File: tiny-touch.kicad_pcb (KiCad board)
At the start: 2 copper layers, 0 parts

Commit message: Begin PCB layout
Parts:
- added 12: Tiny-Touch-Pad, ckeys:Tiny-Touch-Pad, F.Cu at (197.9, 122.4)
- added C1: 1UF, Capacitor_SMD:C_0603_1608Metric_Pad1.05x0.95mm_HandSolder, F.Cu at (262.0, 180.3)
- added C10: 4.7nF, Capacitor_SMD:C_0603_1608Metric_Pad1.05x0.95mm_HandSolder, F.Cu at (243.9, 195.6)
- added C11: 4.7nF, Capacitor_SMD:C_0603_1608Metric_Pad1.05x0.95mm_HandSolder, F.Cu at (257.7, 180.3)
- added C2: 1UF, Capacitor_SMD:C_0603_1608Metric_Pad1.05x0.95mm_HandSolder, F.Cu at (248.3, 193.0)
- added C3: 0.1UF, Capacitor_SMD:C_0603_1608Metric_Pad1.05x0.95mm_HandSolder, F.Cu at (263.1, 173.2)
- added C4: 4.7UF, Capacitor_SMD:C_0603_1608Metric_Pad1.05x0.95mm_HandSolder, F.Cu at (198.1, 204.2)
- added C5: 1UF, Capacitor_SMD:C_0603_1608Metric_Pad1.05x0.95mm_HandSolder, F.Cu at (239.6, 193.0)
- added C6: 10UF, Capacitor_SMD:C_0603_1608Metric_Pad1.05x0.95mm_HandSolder, F.Cu at (239.6, 195.6)
- added C7: 0.1UF, Capacitor_SMD:C_0603_1608Metric_Pad1.05x0.95mm_HandSolder, F.Cu at (258.2, 177.8)
- added C8: 0.1UF, Capacitor_SMD:C_0603_1608Metric_Pad1.05x0.95mm_HandSolder, F.Cu at (243.9, 193.0)
- added C9: 4.7UF, Capacitor_SMD:C_0603_1608Metric_Pad1.05x0.95mm_HandSolder, F.Cu at (262.6, 177.8)
- added D1: RB060M-60TR, ckeys:PMDU, F.Cu at (184.0, 179.8)
- added D2: 1N4148, Diode_SMD:D_SOD-323_HandSoldering, F.Cu at (195.5, 153.8)
- added F1: Tiny-Touch-Pad, ckeys:Tiny-Touch-Pad, F.Cu at (126.3, 122.4)
- added F10: Tiny-Touch-Pad, ckeys:Tiny-Touch-Pad, F.Cu at (184.9, 122.3)
- added F11: Tiny-Touch-Pad, ckeys:Tiny-Touch-Pad, F.Cu at (191.4, 122.4)
- added F2: Tiny-Touch-Pad, ckeys:Tiny-Touch-Pad, F.Cu at (132.8, 122.4)
- added F3: Tiny-Touch-Pad, ckeys:Tiny-Touch-Pad, F.Cu at (139.4, 122.4)
- added F4: Tiny-Touch-Pad, ckeys:Tiny-Touch-Pad, F.Cu at (145.9, 122.4)
- added F5: Tiny-Touch-Pad, ckeys:Tiny-Touch-Pad, F.Cu at (152.4, 122.3)
- added F6: Tiny-Touch-Pad, ckeys:Tiny-Touch-Pad, F.Cu at (158.9, 122.3)
- added F7: Tiny-Touch-Pad, ckeys:Tiny-Touch-Pad, F.Cu at (165.4, 122.3)
- added F8: Tiny-Touch-Pad, ckeys:Tiny-Touch-Pad, F.Cu at (171.9, 122.3)
- added F9: Tiny-Touch-Pad, ckeys:Tiny-Touch-Pad, F.Cu at (178.4, 122.3)
- added H1: Pointer_Clip, ckeys:microbit-clamp-hole-pad, F.Cu at (179.0, 174.2)
- added IC1: STM32F072VBT6, ckeys:QFP50P1600X1600X160-100N, F.Cu at (184.6, 161.3)
- added PAD13: Tiny-Touch-Pad, ckeys:Tiny-Touch-Pad-2u, F.Cu at (206.6, 122.5)
- added PAD14: Tiny-Touch-Pad, ckeys:Tiny-Touch-Pad-2u, F.Cu at (128.6, 129.1)
- added PAD15: Tiny-Touch-Pad, ckeys:Tiny-Touch-Pad-2u, F.Cu at (139.1, 129.1)
- added PAD16: Tiny-Touch-Pad, ckeys:Tiny-Touch-Pad-3u, F.Cu at (156.1, 136.6)
- added PAD17: Tiny-Touch-Pad, ckeys:Tiny-Touch-Pad-1.75u, F.Cu at (170.7, 136.6)
- added PAD18: Tiny-Touch-Pad, ckeys:Tiny-Touch-Pad-1.75u, F.Cu at (149.2, 178.5)
- added PAD19: Tiny-Touch-Pad, ckeys:Tiny-Touch-Pad-1.75u, F.Cu at (158.1, 178.5)
- added PAD20: Tiny-Touch-Pad, ckeys:Tiny-Touch-Pad-1.75u, F.Cu at (156.8, 191.2)
- added PAD21: Tiny-Touch-Pad, ckeys:Tiny-Touch-Pad-2u, F.Cu at (167.2, 188.6)
- added PAD22: Tiny-Touch-Pad, ckeys:Tiny-Touch-Pad-1.5u, F.Cu at (166.0, 196.2)
- added PAD23: Tiny-Touch-Pad, ckeys:Tiny-Touch-Pad-1.5u, F.Cu at (166.0, 202.6)
- added PAD24: Tiny-Touch-Pad, ckeys:Tiny-Touch-Pad-2.25u, F.Cu at (220.5, 152.8)
- added PAD25: Tiny-Touch-Pad, ckeys:Tiny-Touch-Pad-2.25u, F.Cu at (154.5, 209.0)
- added PAD26: Tiny-Touch-Pad, ckeys:Tiny-Touch-Pad-2.25u, F.Cu at (163.4, 209.0)
- added PAD27: Tiny-Touch-Pad, ckeys:Tiny-Touch-Pad-2.25u, F.Cu at (181.6, 198.1)
- added PAD28: Tiny-Touch-Pad, ckeys:Tiny-Touch-Pad, F.Cu at (205.5, 193.5)
- added PAD29: Tiny-Touch-Pad, ckeys:Tiny-Touch-Pad, F.Cu at (240.6, 149.0)
- added PAD30: Tiny-Touch-Pad, ckeys:Tiny-Touch-Pad, F.Cu at (200.5, 197.1)
- added PAD31: Tiny-Touch-Pad, ckeys:Tiny-Touch-Pad, F.Cu at (210.5, 187.4)
- added PAD32: Tiny-Touch-Pad, ckeys:Tiny-Touch-Pad, F.Cu at (224.1, 178.8)
- added PAD33: Tiny-Touch-Pad, ckeys:Tiny-Touch-Pad, F.Cu at (215.5, 187.4)
- added PAD34: Tiny-Touch-Pad, ckeys:Tiny-Touch-Pad, F.Cu at (243.0, 159.4)
- added PAD35: Tiny-Touch-Pad, ckeys:Tiny-Touch-Pad, F.Cu at (238.0, 166.1)
- added PAD36: Tiny-Touch-Pad, ckeys:Tiny-Touch-Pad, F.Cu at (247.0, 149.0)
- added PAD37: Tiny-Touch-Pad, ckeys:Tiny-Touch-Pad, F.Cu at (229.1, 172.7)
- added PAD38: Tiny-Touch-Pad, ckeys:Tiny-Touch-Pad, F.Cu at (210.5, 194.0)
- added PAD39: Tiny-Touch-Pad, ckeys:Tiny-Touch-Pad, F.Cu at (205.5, 200.1)
- added PAD40: Tiny-Touch-Pad, ckeys:Tiny-Touch-Pad, F.Cu at (224.1, 185.4)
- added PAD41: Tiny-Touch-Pad, ckeys:Tiny-Touch-Pad, F.Cu at (215.5, 194.0)
- added PAD42: Tiny-Touch-Pad, ckeys:Tiny-Touch-Pad-1.5u, F.Cu at (199.4, 184.1)
- added PAD43: Tiny-Touch-Pad, ckeys:Tiny-Touch-Pad, F.Cu at (229.1, 179.3)
- added PAD44: Tiny-Touch-Pad, ckeys:Tiny-Touch-Pad, F.Cu at (255.3, 152.8)
- added PAD45: Tiny-Touch-Pad, ckeys:Tiny-Touch-Pad, F.Cu at (243.0, 166.1)
- added PAD46: Tiny-Touch-Pad, ckeys:Tiny-Touch-Pad, F.Cu at (248.0, 159.4)
- added PAD47: Tiny-Touch-Pad, ckeys:Tiny-Touch-Pad, F.Cu at (210.5, 200.6)
- added PAD48: Tiny-Touch-Pad, ckeys:Tiny-Touch-Pad, F.Cu at (239.1, 172.7)
- added PAD49: Tiny-Touch-Pad, ckeys:Tiny-Touch-Pad, F.Cu at (220.5, 192.0)
- added PAD50: Tiny-Touch-Pad, ckeys:Tiny-Touch-Pad, F.Cu at (215.5, 200.6)
- added PAD51: Tiny-Touch-Pad, ckeys:Tiny-Touch-Pad, F.Cu at (253.0, 159.4)
- added PAD52: Tiny-Touch-Pad, ckeys:Tiny-Touch-Pad, F.Cu at (248.0, 166.1)
- added PAD53: Tiny-Touch-Pad, ckeys:Tiny-Touch-Pad, F.Cu at (260.3, 152.8)
- added PAD54: Tiny-Touch-Pad, ckeys:Tiny-Touch-Pad-1.5u, F.Cu at (208.4, 174.1)
- added PAD55: Tiny-Touch-Pad, ckeys:Tiny-Touch-Pad-1.75u, F.Cu at (207.5, 167.8)
- added PAD56: Tiny-Touch-Pad, ckeys:Tiny-Touch-Pad, F.Cu at (258.0, 159.4)
- added PAD57: Tiny-Touch-Pad, ckeys:Tiny-Touch-Pad, F.Cu at (244.1, 172.7)
- added PAD58: Tiny-Touch-Pad, ckeys:Tiny-Touch-Pad, F.Cu at (239.1, 179.3)
- added PAD59: Tiny-Touch-Pad, ckeys:Tiny-Touch-Pad, F.Cu at (265.3, 152.8)
- added PAD60: Tiny-Touch-Pad, ckeys:Tiny-Touch-Pad, F.Cu at (220.5, 198.6)
- added PAD61: Tiny-Touch-Pad, ckeys:Tiny-Touch-Pad, F.Cu at (253.0, 166.1)
- added PAD62: Tiny-Touch-Pad, ckeys:Tiny-Touch-Pad, F.Cu at (249.1, 172.7)
- added PAD63: Tiny-Touch-Pad, ckeys:Tiny-Touch-Pad, F.Cu at (263.0, 159.4)
- added PAD64: Tiny-Touch-Pad, ckeys:Tiny-Touch-Pad, F.Cu at (234.1, 185.9)
- added PAD65: Tiny-Touch-Pad, ckeys:Tiny-Touch-Pad, F.Cu at (225.5, 192.5)
- added PAD66: Tiny-Touch-Pad, ckeys:Tiny-Touch-Pad, F.Cu at (258.0, 166.1)
- added PAD67: Tiny-Touch-Pad, ckeys:Tiny-Touch-Pad-1.25u, F.Cu at (268.7, 166.1)
- added PAD68: Tiny-Touch-Pad, ckeys:Tiny-Touch-Pad-2.25u, F.Cu at (187.9, 171.3)
- added PAD69: Tiny-Touch-Pad, ckeys:Tiny-Touch-Pad, F.Cu at (244.1, 179.3)
- added PAD70: Tiny-Touch-Pad, ckeys:Tiny-Touch-Pad, F.Cu at (239.1, 185.9)
- added PAD71: Tiny-Touch-Pad, ckeys:Tiny-Touch-Pad, F.Cu at (225.5, 199.2)
- added PAD72: Tiny-Touch-Pad, ckeys:Tiny-Touch-Pad, F.Cu at (249.1, 179.3)
- added PAD73: Tiny-Touch-Pad, ckeys:Tiny-Touch-Pad, F.Cu at (235.5, 192.5)
- added PAD74: Tiny-Touch-Pad, ckeys:Tiny-Touch-Pad, F.Cu at (268.0, 159.4)
- added PAD75: Tiny-Touch-Pad, ckeys:Tiny-Touch-Pad, F.Cu at (254.1, 172.7)
- added PAD76: Tiny-Touch-Pad, ckeys:Tiny-Touch-Pad, F.Cu at (263.0, 166.1)
- added PAD77: Tiny-Touch-Pad, ckeys:Tiny-Touch-Pad, F.Cu at (230.5, 199.2)
- added PAD78: Tiny-Touch-Pad, ckeys:Tiny-Touch-Pad, F.Cu at (244.1, 185.9)
- added PAD79: Tiny-Touch-Pad, ckeys:Tiny-Touch-Pad-1.75u, F.Cu at (216.5, 161.4)
- added PAD80: Tiny-Touch-Pad, ckeys:Tiny-Touch-Pad, F.Cu at (235.5, 199.2)
- added PAD81: Tiny-Touch-Pad, ckeys:Tiny-Touch-Pad, F.Cu at (249.1, 185.9)
- added PAD82: Tiny-Touch-Pad, ckeys:Tiny-Touch-Pad, F.Cu at (270.3, 152.8)
- added PAD83: Tiny-Touch-Pad, ckeys:Tiny-Touch-Pad, F.Cu at (230.5, 192.5)
- added PAD84: Tiny-Touch-Pad, ckeys:Tiny-Touch-Pad, F.Cu at (229.1, 185.9)
- added PAD85: Tiny-Touch-Pad, ckeys:Tiny-Touch-Pad-3u, F.Cu at (199.2, 156.4)
- added PAD86: Tiny-Touch-Pad, ckeys:Tiny-Touch-Pad, F.Cu at (234.1, 179.3)
- added PAD87: Tiny-Touch-Pad, ckeys:Tiny-Touch-Pad, F.Cu at (234.1, 172.7)
- added PAD88: Tiny-Touch-Pad, ckeys:Tiny-Touch-Pad, F.Cu at (219.0, 178.2)
- added PAD89: Tiny-Touch-Pad, ckeys:Tiny-Touch-Pad, F.Cu at (233.0, 166.1)
- added PAD90: Tiny-Touch-Pad, ckeys:Tiny-Touch-Pad, F.Cu at (238.0, 159.4)
- added PAD91: Tiny-Touch-Pad, ckeys:Tiny-Touch-Pad, F.Cu at (224.1, 172.1)
- added PF1: 500mA, Fuse:Fuse_1206_3216Metric_Pad1.42x1.75mm_HandSolder, F.Cu at (189.0, 191.3)
- added Q1: DTC123J, ckeys:SOT65P210X100-3N, F.Cu at (193.6, 204.8)
- added R1: 100K, Resistor_SMD:R_0603_1608Metric_Pad1.05x0.95mm_HandSolder, F.Cu at (267.4, 173.1)
- added R2: 100K, Resistor_SMD:R_0603_1608Metric_Pad1.05x0.95mm_HandSolder, F.Cu at (257.7, 182.8)
- added R3: 1M, Resistor_SMD:R_0603_1608Metric_Pad1.05x0.95mm_HandSolder, F.Cu at (239.6, 198.1)
- added R4: 100K, Resistor_SMD:R_0603_1608Metric_Pad1.05x0.95mm_HandSolder, F.Cu at (253.2, 184.3)
- added R5: 5k1, Resistor_SMD:R_0603_1608Metric_Pad1.05x0.95mm_HandSolder, F.Cu at (253.2, 186.9)
- added R6: 5k1, Resistor_SMD:R_0603_1608Metric_Pad1.05x0.95mm_HandSolder, F.Cu at (239.6, 200.6)
- added SW1: SW_Push, Button_Switch_SMD:SW_Push_1P1T_NO_6x6mm_H9.5mm, F.Cu at (206.7, 154.1)
- added U1: MCP1700-3002E_SOT23, Package_TO_SOT_SMD:SOT-23, F.Cu at (253.3, 180.8)
- added U2: SRV05-4, Package_TO_SOT_SMD:SOT-23-6, F.Cu at (258.5, 174.2)
- added USB1: HRO-TYPE-C-31-M-12, Type-C:HRO-TYPE-C-31-M-12-HandSoldering, F.Cu at (180.7, 192.8)

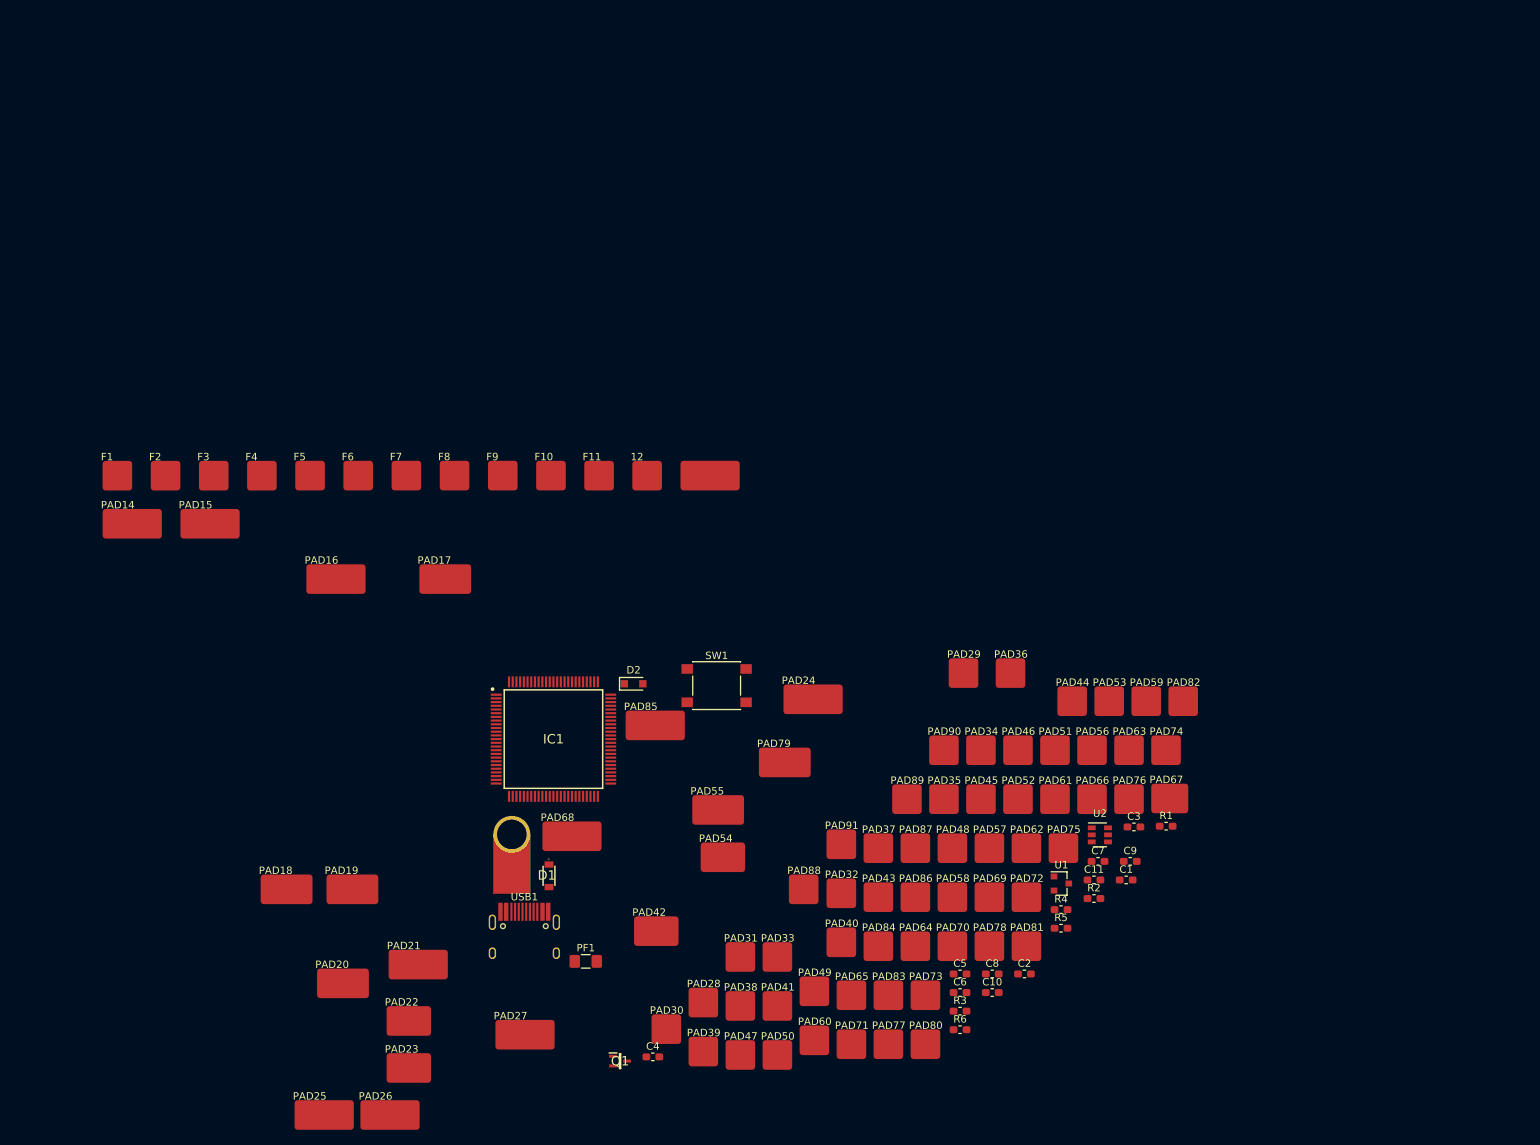
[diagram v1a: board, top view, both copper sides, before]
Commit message: Fix footprint size/spacing
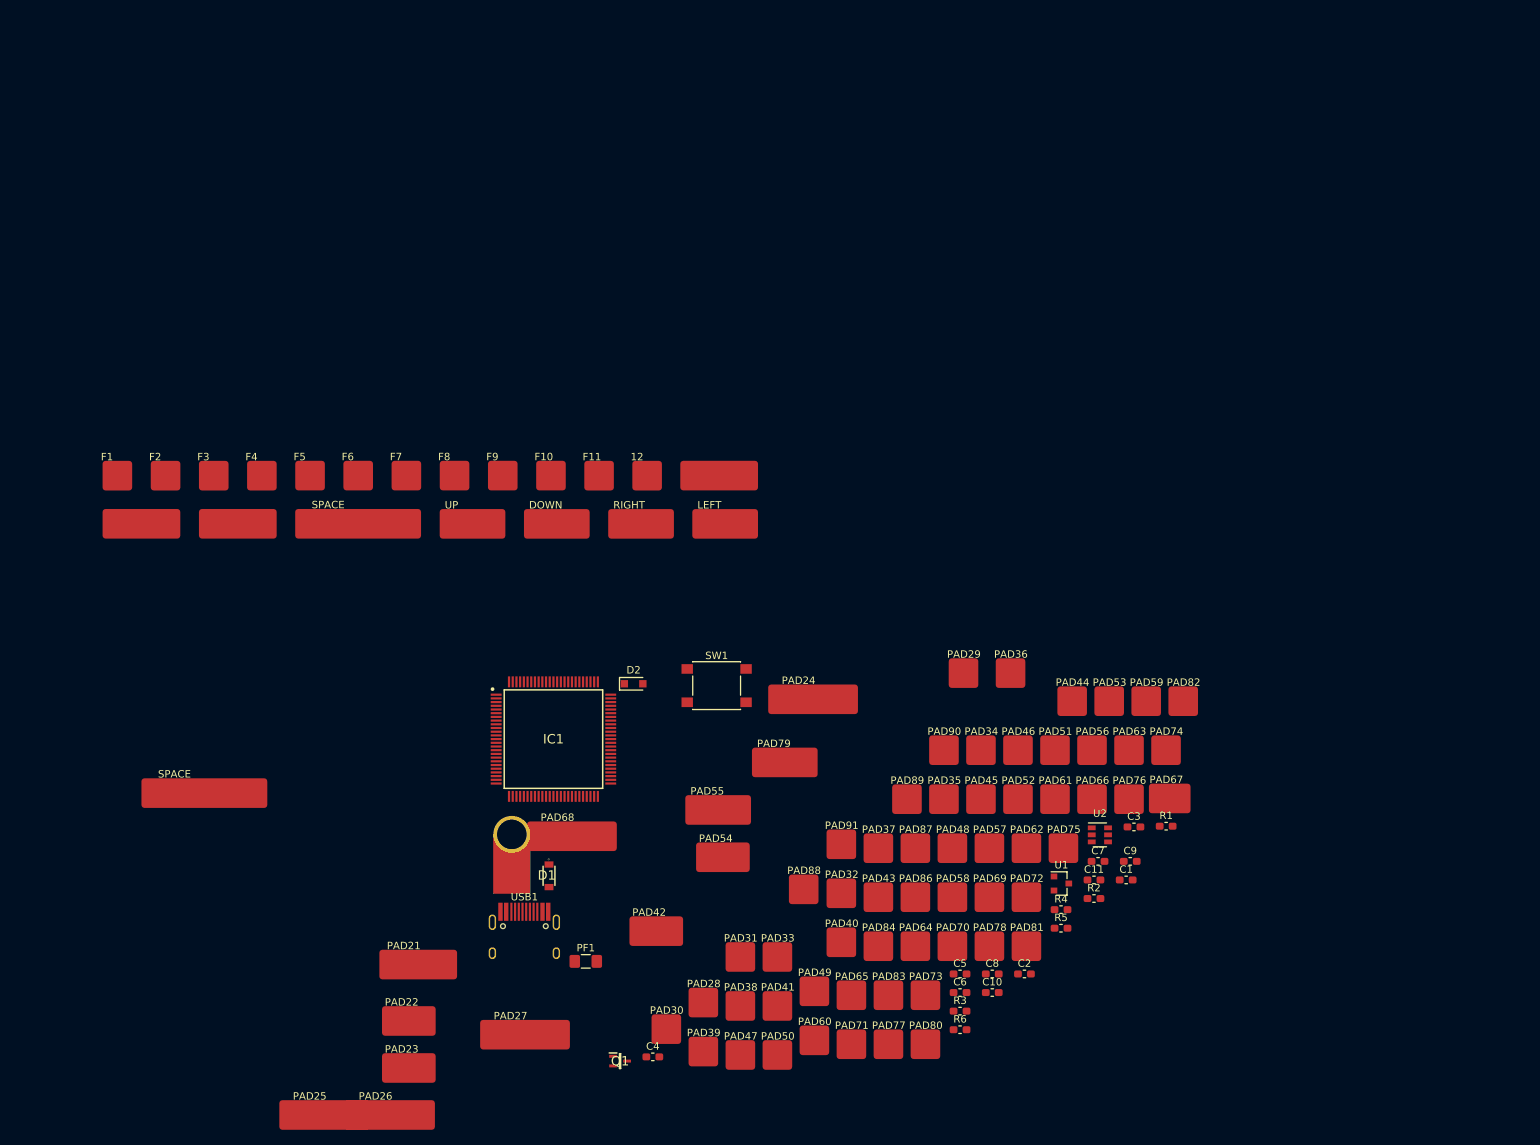
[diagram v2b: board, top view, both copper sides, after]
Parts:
- removed PAD20: Tiny-Touch-Pad, ckeys:Tiny-Touch-Pad-1.75u
- added LEFT: Tiny-Touch-Pad, ckeys:Tiny-Touch-Pad-1.75u, F.Cu at (208.5, 129.1)
- moved RIGHT 62.9 mm to (197.1, 129.1)
- moved SPACE 61.6 mm to (138.3, 165.5)
- moved DOWN 61.4 mm to (185.7, 129.1)
- moved UP 8.32 mm to (174.3, 129.1)
- moved SPACE 8.05 mm to (159.1, 129.1)
- moved PAD15 3.75 mm to (142.8, 129.1)
- moved PAD14 1.24 mm to (129.8, 129.1)
- moved PAD13 1.22 mm to (207.8, 122.5)
- renumbered PAD18 to DOWN, PAD19 to RIGHT, PAD16 to SPACE, PAD85 to SPACE, PAD17 to UP

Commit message: Complete layout of keys
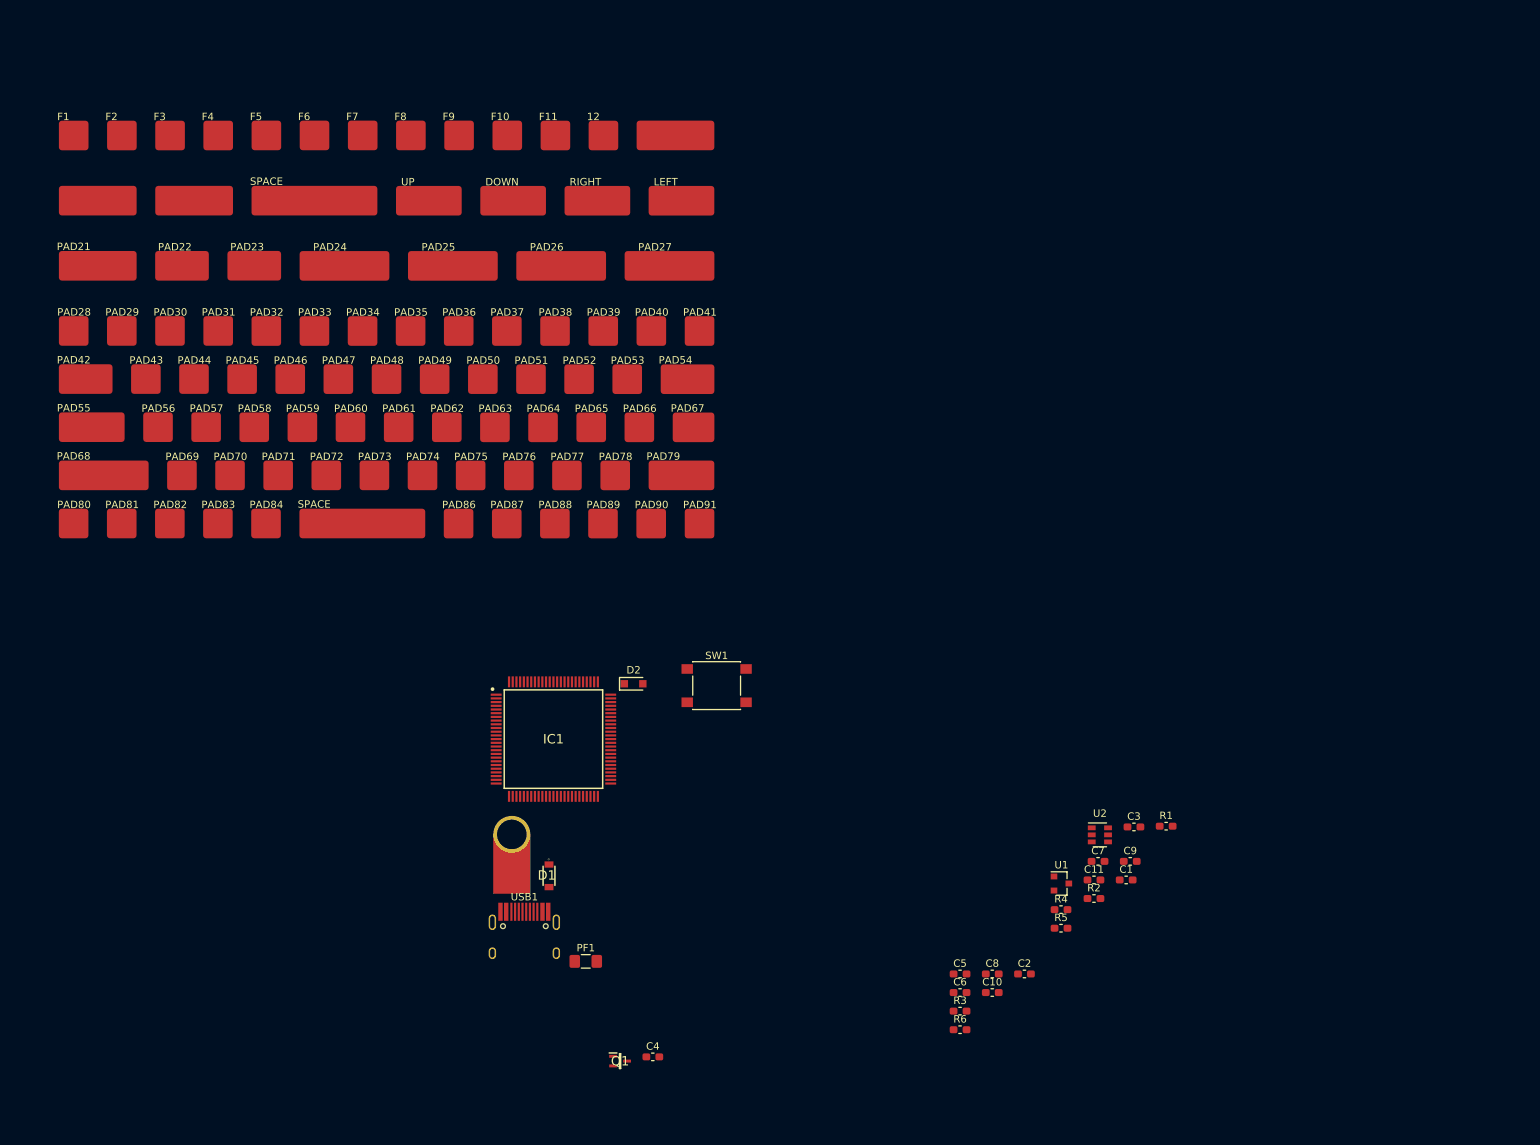
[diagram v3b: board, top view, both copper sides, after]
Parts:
- moved PAD82 139.0 mm to (133.4, 128.8)
- moved PAD81 134.9 mm to (126.9, 128.8)
- moved PAD80 134.9 mm to (120.4, 128.8)
- moved PAD56 133.5 mm to (131.8, 115.8)
- moved PAD44 126.4 mm to (136.7, 109.3)
- moved PAD28 124.4 mm to (120.4, 102.8)
- moved PAD69 123.1 mm to (135.1, 122.3)
- moved PAD29 122.7 mm to (126.9, 102.8)
- moved PAD43 121.2 mm to (130.2, 109.3)
- moved PAD57 120.1 mm to (138.3, 115.8)
- moved PAD59 119.8 mm to (151.3, 115.8)
- moved PAD26 117.0 mm to (186.5, 94.3)
- moved PAD70 116.5 mm to (141.6, 122.3)
- moved PAD25 116.0 mm to (171.9, 94.3)
- moved PAD30 115.7 mm to (133.4, 102.8)
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
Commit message: Rename all switches on PCB
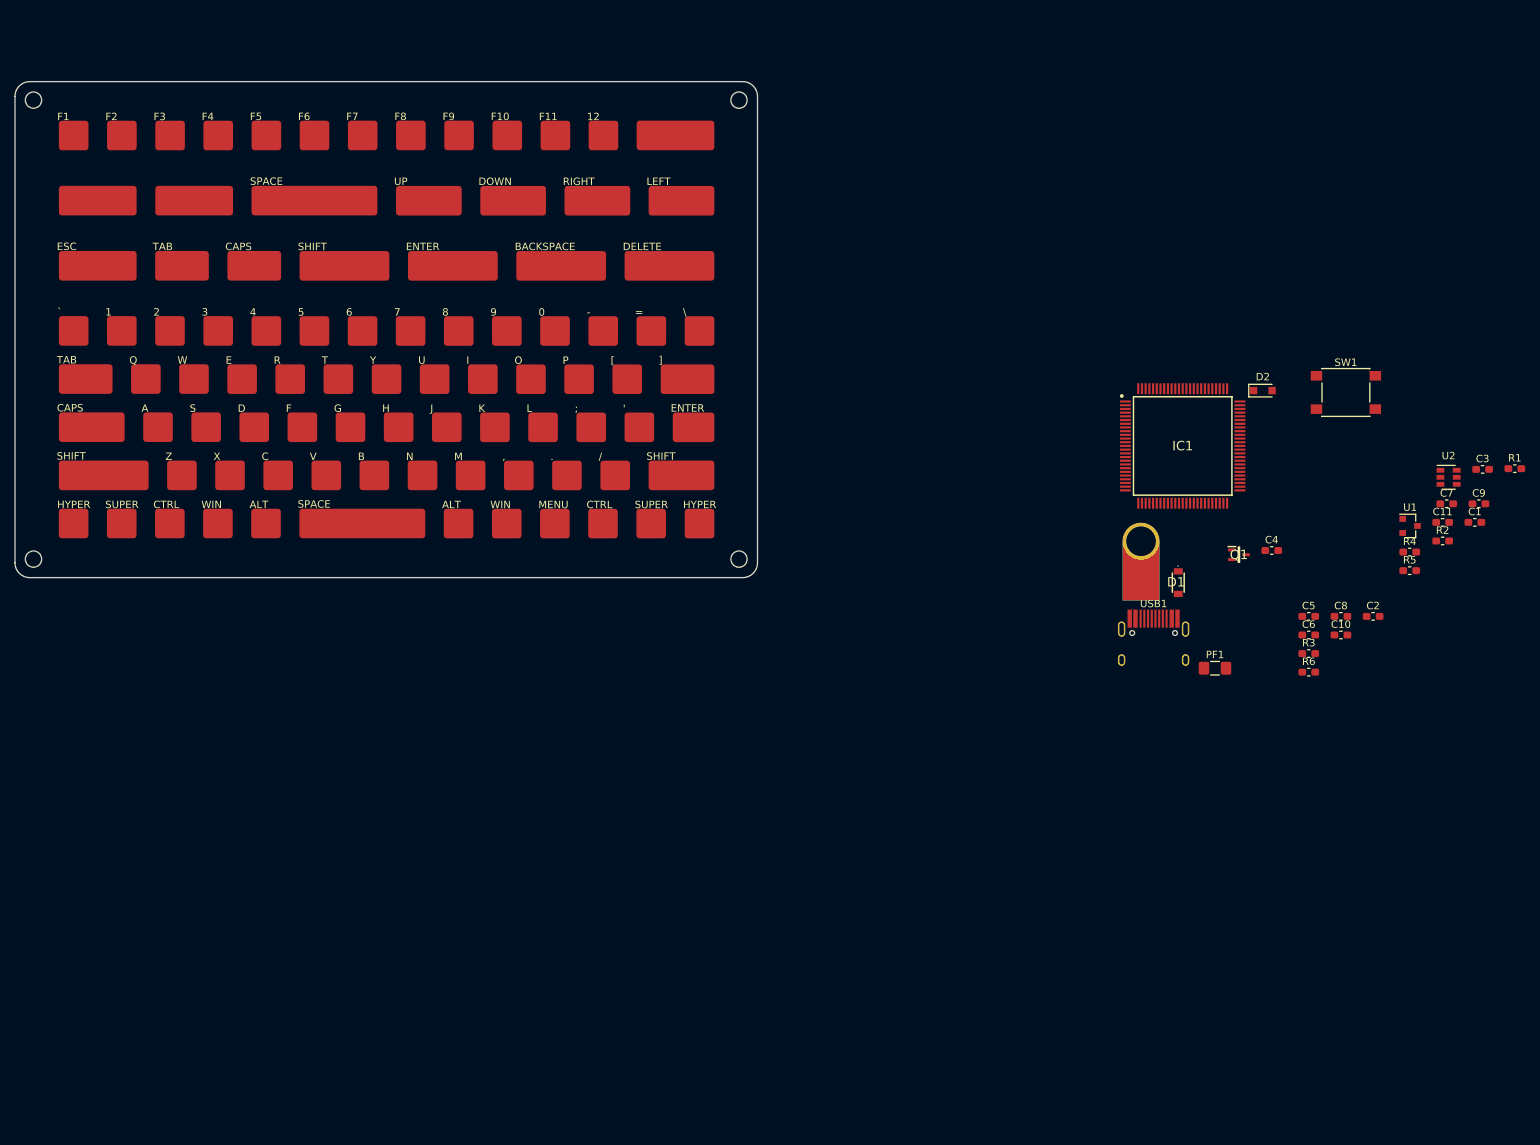
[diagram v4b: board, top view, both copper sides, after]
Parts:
- added REF**: MountingHole_2.2mm_M2, MountingHole:MountingHole_2.2mm_M2, F.Cu at (114.4, 137.0)
- added REF**: MountingHole_2.2mm_M2, MountingHole:MountingHole_2.2mm_M2, F.Cu at (114.4, 75.0)
- added REF**: MountingHole_2.2mm_M2, MountingHole:MountingHole_2.2mm_M2, F.Cu at (209.7, 137.0)
- added REF**: MountingHole_2.2mm_M2, MountingHole:MountingHole_2.2mm_M2, F.Cu at (209.7, 75.0)
- moved C4 108.0 mm to (281.7, 135.8)
- moved Q1 108.0 mm to (277.2, 136.4)
- moved USB1 93.8 mm to (265.7, 153.2)
- moved H1 93.8 mm to (264.0, 134.6)
- moved IC1 93.8 mm to (269.6, 121.7)
- moved D2 93.8 mm to (280.5, 114.2)
- moved D1 93.8 mm to (269.0, 140.2)
- moved PF1 93.8 mm to (274.0, 151.7)
- moved SW1 93.8 mm to (291.7, 114.5)
- moved C1 67.5 mm to (309.1, 132.0)
- moved C10 67.5 mm to (291.0, 147.2)
- moved C3 67.5 mm to (310.2, 124.9)
- moved C9 67.5 mm to (309.7, 129.5)
- moved C6 67.5 mm to (286.7, 147.2)
- moved C8 67.5 mm to (291.0, 144.7)
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- renumbered PAD66 to ', PAD76 to ,, PAD39 to -, PAD77 to ., PAD78 to /, PAD38 to 0, PAD29 to 1, PAD30 to 2, PAD31 to 3, PAD32 to 4, PAD33 to 5, PAD34 to 6, PAD35 to 7, PAD36 to 8, PAD37 to 9, PAD65 to ;, PAD40 to =, PAD56 to A, PAD86 to ALT, PAD84 to ALT, PAD73 to B, PAD26 to BACKSPACE, PAD71 to C, PAD23 to CAPS, PAD55 to CAPS, PAD89 to CTRL, PAD82 to CTRL, PAD58 to D, PAD27 to DELETE, PAD45 to E, PAD25 to ENTER, PAD67 to ENTER, PAD21 to ESC, PAD59 to F, PAD60 to G, PAD61 to H, PAD91 to HYPER, PAD80 to HYPER, PAD50 to I, PAD62 to J, PAD63 to K, PAD64 to L, PAD75 to M, PAD88 to MENU, PAD74 to N, PAD51 to O, PAD52 to P, PAD43 to Q, PAD46 to R, PAD57 to S, PAD79 to SHIFT, PAD68 to SHIFT, PAD24 to SHIFT, PAD90 to SUPER, PAD81 to SUPER, PAD47 to T, PAD22 to TAB, PAD42 to TAB, PAD49 to U, PAD72 to V, PAD44 to W, PAD87 to WIN, PAD83 to WIN, PAD70 to X, PAD48 to Y, PAD69 to Z, PAD53 to [, PAD41 to \, PAD54 to ], PAD28 to `
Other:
- board outline added: 100.3 x 67 mm
